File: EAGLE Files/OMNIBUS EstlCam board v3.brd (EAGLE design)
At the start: 100.6 x 73.6 mm, 67 parts, among them K1 691131710002, K2 691131710003, K3 691131710003, K4 691131710003, U1 LTV-847S, U2 L7805ACD2T-TR, U3 LM358M/NOPB, U4 LTV-847S, U5 PC817X3NSZ1B, U6 ULN2003AD, U7 L78L05ACU, U8 74AHC1G125

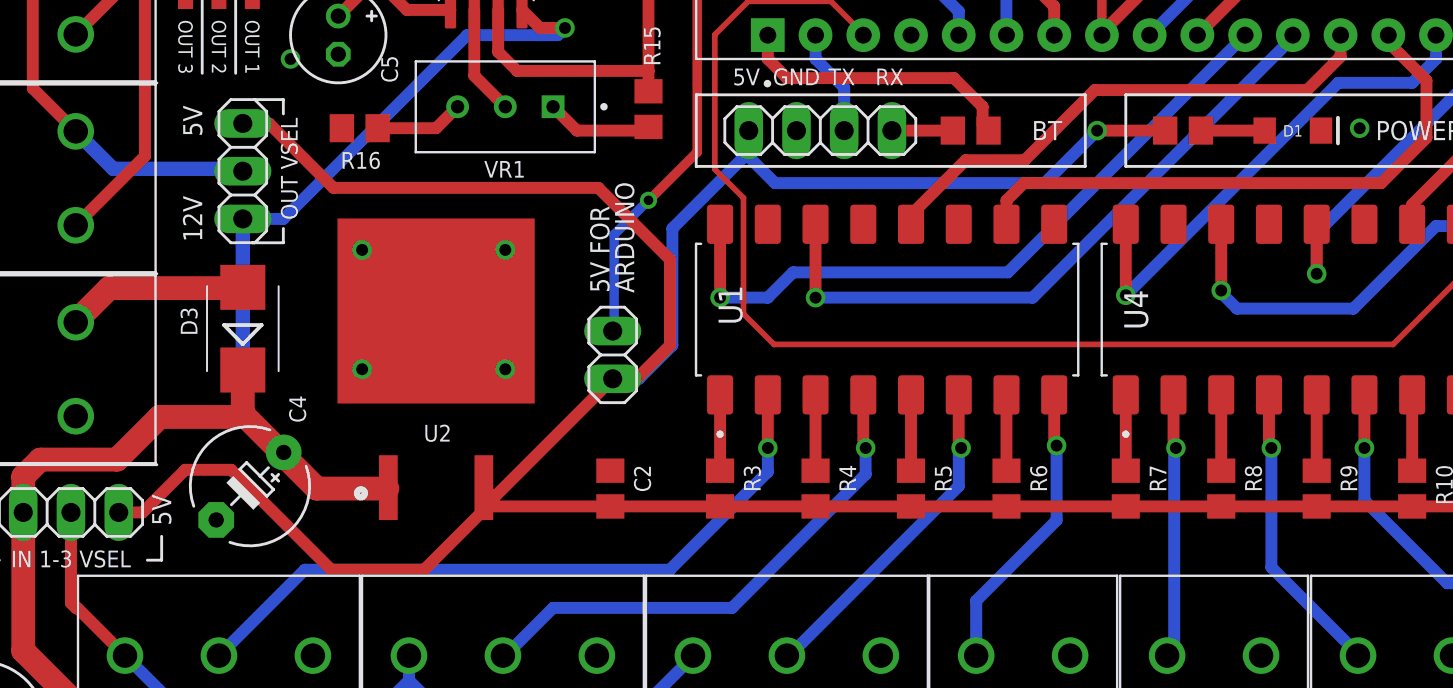
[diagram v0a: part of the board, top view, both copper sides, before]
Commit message: PCB Bugfixes and polishing
• DRV Shield had an routing error (laser indicator LED) also R3 had a wrong value
• New Footprint for the 0.33uF Caps
• Silkscreen polishing
• almost all LEDs are 0805 package now
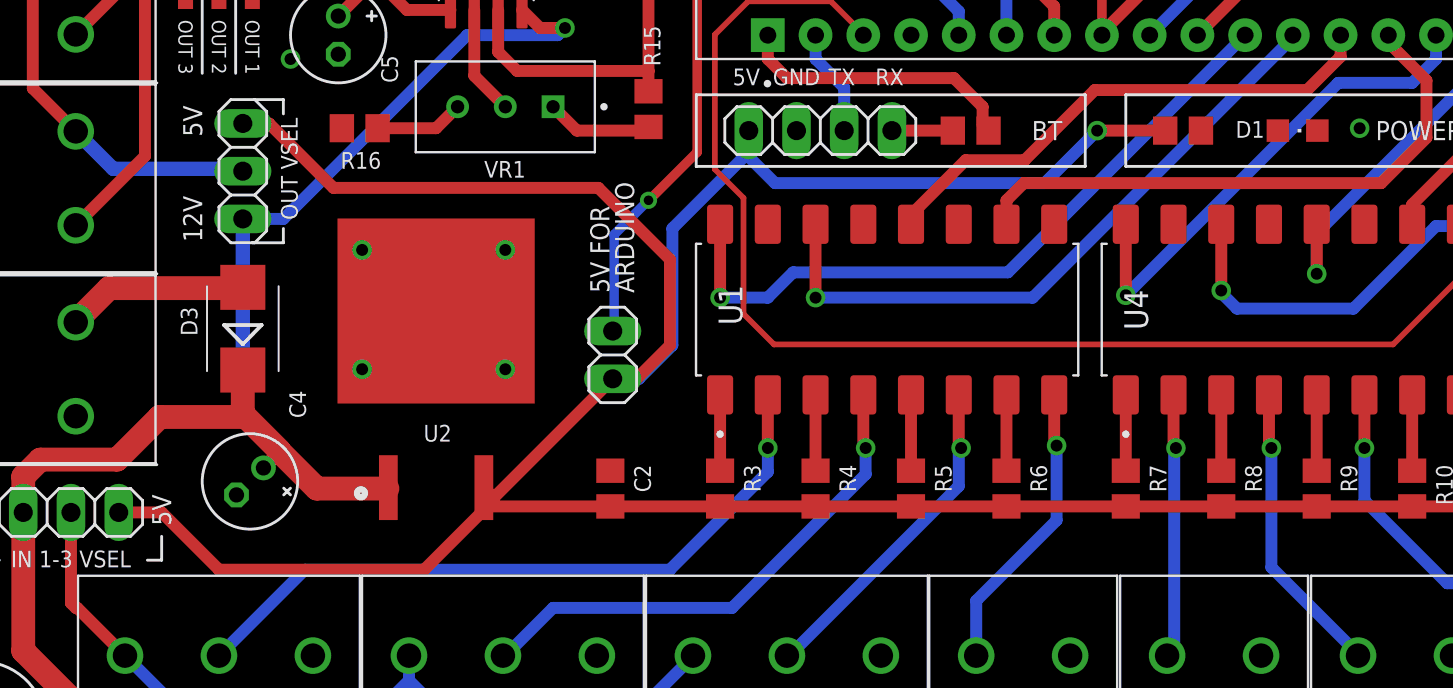
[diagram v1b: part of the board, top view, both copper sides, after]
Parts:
- C4: value 220uf 25v -> 0.33uf 25v; device rcl:E5-6 -> rcl:E2-5
- D1: value (none) -> green; device SparkFun-LED:LED-1206 -> led:CHIPLED_0805
- moved D1 0.25 mm to (72.6, 35.6), turned to 270 degrees
- moved C4 0.25 mm to (16.9, 16.9)
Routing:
- net N$1: track 3.39 -> 0.00 mm
- net 12V: track 254.8 -> 258.2 mm
- net 5V: track 209.0 -> 207.1 mm
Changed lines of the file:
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@@
 <attribute name="VALUE" x="19.177" y="38.227" size="1.27" layer="27" ratio="10" rot="R270"/>
 </element>
-<element name="C4" library="rcl" library_urn="urn:adsk.eagle:library:334" package="E5-6" package3d_urn="urn:adsk.eagle:package:23368/1" value="220uf 25v" x="16.891" y="16.637" smashed="yes" rot="R225">
-<attribute name="NAME" x="19.873628125" y="20.005915625" size="0.889" layer="25" font="vector" ratio="10" rot="R90"/>
-<attribute name="POPULARITY" value="2" x="16.891" y="16.637" size="1.778" layer="27" rot="R225" display="off"/>
-<attribute name="SPICEPREFIX" value="C" x="16.891" y="16.637" size="1.778" layer="27" rot="R225" display="off"/>
-<attribute name="VALUE" x="13.2989" y="16.637" size="1.27" layer="27" ratio="10" rot="R225"/>
+<element name="C4" library="rcl" library_urn="urn:adsk.eagle:library:334" package="E2-5" package3d_urn="urn:adsk.eagle:package:23346/2" value="0.33uf 25v" x="16.891" y="16.891" smashed="yes" rot="R225">
+<attribute name="NAME" x="19.873628125" y="20.259915625" size="0.889" layer="25" font="vector" ratio="10" rot="R90"/>
+<attribute name="POPULARITY" value="14" x="16.891" y="16.891" size="1.778" layer="27" rot="R225" display="off"/>
+<attribute name="SPICEPREFIX" value="C" x="16.891" y="16.891" size="1.778" layer="27" rot="R225" display="off"/>
+<attribute name="VALUE" x="13.2989" y="16.891" size="1.27" layer="27" ratio="10" rot="R225"/>
 </element>
 <element name="RESET" library="con-molex" library_urn="urn:adsk.eagle:library:165" package="22-23-2021" package3d_urn="urn:adsk.eagle:package:8078633/1" value="22-23-2021" x="87.63" y="58.42" smashed="yes" rot="R270">
@@
 <attribute name="POPULARITY" value="40" x="87.63" y="58.42" size="1.778" layer="27" rot="R270" display="off"/>
 <attribute name="VALUE" x="82.55" y="60.96" size="1.016" layer="27" ratio="10" rot="R270"/>
-</element>
-<element name="D1" library="SparkFun-LED" library_urn="urn:adsk.eagle:library:529" package="LED-1206" package3d_urn="urn:adsk.eagle:package:39352/1" value="" x="72.39" y="35.56" smashed="yes">
-<attribute name="NAME" x="72.39" y="35.2425" size="0.6096" layer="25" font="vector" ratio="20" align="bottom-center"/>
-<attribute name="VALUE" x="72.39" y="34.6075" size="0.6096" layer="27" font="vector" ratio="20" align="top-center"/>
 </element>
 <element name="R1" library="rcl" library_urn="urn:adsk.eagle:library:334" package="R0805" package3d_urn="urn:adsk.eagle:package:23553/2" value="1k" x="55.245" y="35.56" smashed="yes" rot="R180">
@@
 <attribute name="POPULARITY" value="98" x="36.195" y="23.622" size="1.778" layer="27" rot="R270" display="off"/>
 <attribute name="VALUE" x="33.02" y="26.162" size="1.27" layer="27" rot="R270"/>
+</element>
+<element name="D1" library="led" library_urn="urn:adsk.eagle:library:259" package="CHIPLED_0805" package3d_urn="urn:adsk.eagle:package:15821/2" value="green" x="72.644" y="35.56" smashed="yes" rot="R270">
+<attribute name="NAME" x="69.342" y="35.179" size="0.889" layer="25" font="vector" ratio="10"/>
+<attribute name="VALUE" x="71.374" y="33.02" size="1.27" layer="27"/>
 </element>
 </elements>
@@
 <contactref element="C4" pad="-"/>
 <contactref element="RESET" pad="1"/>
-<contactref element="D1" pad="C"/>
 <contactref element="BT" pad="3"/>
 <contactref element="ON_OFF2" pad="1"/>
@@
 <via x="75.946" y="35.687" extent="1-16" drill="0.635"/>
 <via x="19.05" y="39.37" extent="1-16" drill="0.635"/>
+<contactref element="D1" pad="C"/>
 </signal>
 <signal name="12V" class="1">
@@
 <wire x1="5.7325" y1="18.0515" x2="4.826" y2="17.145" width="1.27" layer="1"/>
 <wire x1="16.51" y1="30.861" x2="16.51" y2="20.437075" width="0.762" layer="16"/>
-<wire x1="18.68705" y1="18.43305" x2="18.66759375" y2="18.43305" width="0.635" layer="16"/>
-<wire x1="18.66759375" y1="18.43305" x2="16.51" y2="20.437075" width="0.762" layer="16"/>
+<wire x1="17.60941875" y1="17.60941875" x2="18.53715" y2="18.554209375" width="0.635" layer="16"/>
+<wire x1="18.53715" y1="18.554209375" x2="16.51" y2="20.437075" width="0.762" layer="16"/>
 <wire x1="81.24" y1="63.5" x2="83.82" y2="60.92" width="0.635" layer="1"/>
 <wire x1="83.82" y1="54.232" x2="79.502" y2="49.914" width="0.635" layer="1"/>
@@
 <wire x1="18.669" y1="30.861" x2="28.448" y2="40.64" width="0.635" layer="16"/>
 <wire x1="28.448" y1="40.64" x2="33.274" y2="40.64" width="0.635" layer="16"/>
-<wire x1="18.56005" y1="18.43305" x2="18.68705" y2="18.43305" width="0.635" layer="1"/>
-<wire x1="18.56005" y1="18.43305" x2="16.6731" y2="20.32" width="1.27" layer="1"/>
+<wire x1="18.441003125" y1="18.552096875" x2="17.60941875" y2="17.60941875" width="0.635" layer="1"/>
+<wire x1="18.441003125" y1="18.552096875" x2="16.6731" y2="20.32" width="1.27" layer="1"/>
 <wire x1="12.0839" y1="20.32" x2="16.4191" y2="20.32" width="1.27" layer="1"/>
 <wire x1="16.4191" y1="20.32" x2="16.6731" y2="20.32" width="0.635" layer="1"/>
-<wire x1="20.447" y1="16.51" x2="18.68705" y2="18.26995" width="1.27" layer="1"/>
-<wire x1="18.68705" y1="18.43305" x2="18.68705" y2="18.26995" width="0.635" layer="1"/>
+<wire x1="20.447" y1="16.51" x2="18.549653125" y2="18.407346875" width="1.27" layer="1"/>
+<wire x1="17.60941875" y1="17.60941875" x2="18.549653125" y2="18.407346875" width="0.635" layer="1"/>
 <wire x1="16.51" y1="22.819" x2="16.51" y2="20.4109" width="1.27" layer="1"/>
 <wire x1="16.51" y1="20.4109" x2="16.4191" y2="20.32" width="0.635" layer="1"/>
@@
 <wire x1="83.886" y1="15.56" x2="87.376" y2="19.05" width="0.635" layer="1"/>
 <wire x1="87.376" y1="19.05" x2="90.297" y2="19.05" width="0.635" layer="1"/>
-<wire x1="21.209" y1="12.192" x2="15.89305" y2="17.50795" width="0.635" layer="1"/>
-<wire x1="13.44395" y1="17.50795" x2="11.176" y2="15.24" width="0.635" layer="1"/>
-<wire x1="11.176" y1="15.24" x2="9.906" y2="15.24" width="0.635" layer="1"/>
-<wire x1="26.162" y1="12.192" x2="21.209" y2="12.192" width="0.635" layer="1"/>
-<wire x1="15.89305" y1="17.50795" x2="13.44395" y2="17.50795" width="0.635" layer="1"/>
+<wire x1="15.24" y1="12.192" x2="12.192" y2="15.24" width="0.635" layer="1"/>
+<wire x1="26.162" y1="12.192" x2="15.24" y2="12.192" width="0.635" layer="1"/>
+<wire x1="12.192" y1="15.24" x2="9.906" y2="15.24" width="0.635" layer="1"/>
 </signal>
 <signal name="N$1">
 <contactref element="R2" pad="2"/>
 <contactref element="D1" pad="A"/>
-<wire x1="67.498" y1="35.56" x2="70.89" y2="35.56" width="0.635" layer="1"/>
+<wire x1="67.498" y1="35.56" x2="71.594" y2="35.56" width="0" layer="19" extent="1-1"/>
 </signal>
 <signal name="IN_VCC" class="1">

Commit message: Changed voltage regulators
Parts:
- U2: value L7805ACD2T-TR -> MC7805C
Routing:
- net N$1: track 0.00 -> 4.10 mm
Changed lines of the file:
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@@
 <attribute name="PURCHASE-URL" value="https://pricing.snapeda.com/search/part/LTV-847S/?ref=eda" x="63.5" y="67.945" size="1.778" layer="27" rot="R90" display="off"/>
 </element>
-<element name="U2" library="L7805ACD2T-TR" package="TO254P1515X470-3N" value="L7805ACD2T-TR" x="26.797" y="22.86" smashed="yes" rot="R90">
+<element name="U2" library="L7805ACD2T-TR" package="TO254P1515X470-3N" value="MC7805C" x="26.797" y="22.86" smashed="yes" rot="R90">
 <attribute name="AVAILABILITY" value="Good" x="90.297" y="46.99" size="1.778" layer="27" rot="R90" display="off"/>
 <attribute name="DESCRIPTION" value=" Linear Voltage Regulator IC Positive Fixed 1 Output 1.5A D2PAK " x="90.297" y="46.99" size="1.778" layer="27" rot="R90" display="off"/>
@@
 <contactref element="R2" pad="2"/>
 <contactref element="D1" pad="A"/>
-<wire x1="67.498" y1="35.56" x2="71.594" y2="35.56" width="0" layer="19" extent="1-1"/>
+<wire x1="67.498" y1="35.56" x2="71.594" y2="35.56" width="0.3048" layer="1"/>
 </signal>
 <signal name="IN_VCC" class="1">

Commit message: clean up
also added BOM
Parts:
- removed K2: 691131710003, Wurth_Terminal_Blocks_Connectors_rev15d:691131710003
- removed PWM_OUT: 691131710002, Wurth_Terminal_Blocks_Connectors_rev15d:691131710002
- added POPW, RPM: KF301-2P, Wurth_Terminal_Blocks_Connectors_rev15d:691131710002
- BT, IN_V_SEL, JP1, OUT_V_SEL: value (none) -> PINHEAD
- DIR1, DIR2, IN4, IN5, IN6, IN7, IN8, OUT1, OUT2, OUT3, PWM, VFD: value 691131710002 -> KF301-2P
- FEED, SPEED: value 22-23-2031 -> JST XH
- IN1: value 691131710002 -> KF301-3P; device Wurth_Terminal_Blocks_Connectors_rev15d:691131710002 -> Wurth_Terminal_Blocks_Connectors_rev15d:691131710003
- IN2, IN3, STEP: value 691131710003 -> KF301-3P
- RESET: value 22-23-2021 -> JST XH
- moved IN1 84.6 mm to (15.2, 7.62)
- moved PWM 10.2 mm to (12.7, 63.5)
- renumbered K3 to IN2, K4 to IN3, ON_OFF to VFD, ON_OFF1 to DIR2, ON_OFF2 to DIR1, ON_OFF3 to OUT1, ON_OFF4 to OUT2, ON_OFF5 to OUT3
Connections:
- net 12V: now also POPW.2; no longer IN1.2
- net GND: now also IN1.3, POPW.1, RPM.1; no longer IN1.1, K2.3, PWM_OUT.1
- net INPUT1: now also IN1.2; no longer K2.2
- net IN_VCC: now also IN1.1; no longer K2.1
- net PWM_10V: now also RPM.2; no longer PWM.2
- net SPINDLE_PWM: now also PWM.2; no longer PWM_OUT.2
